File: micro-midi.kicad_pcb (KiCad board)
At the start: 2 copper layers, 36 x 39 mm, 14 parts, among them J1 AudioJack3, J2 Conn_01x04_Male, J3 AudioJack3, U1 74HC04, U2 6N137

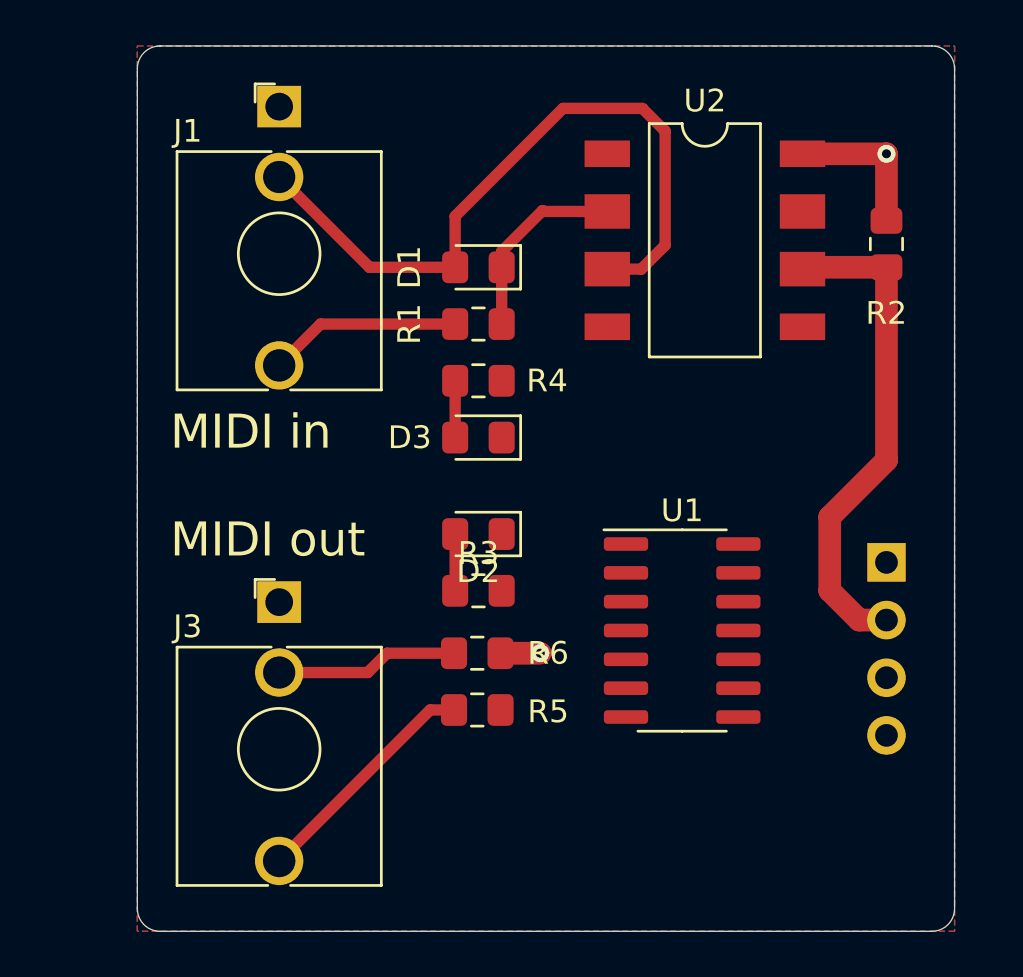
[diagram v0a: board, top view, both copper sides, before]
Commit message: finish pcb routing, clean up component numbers silkscreen
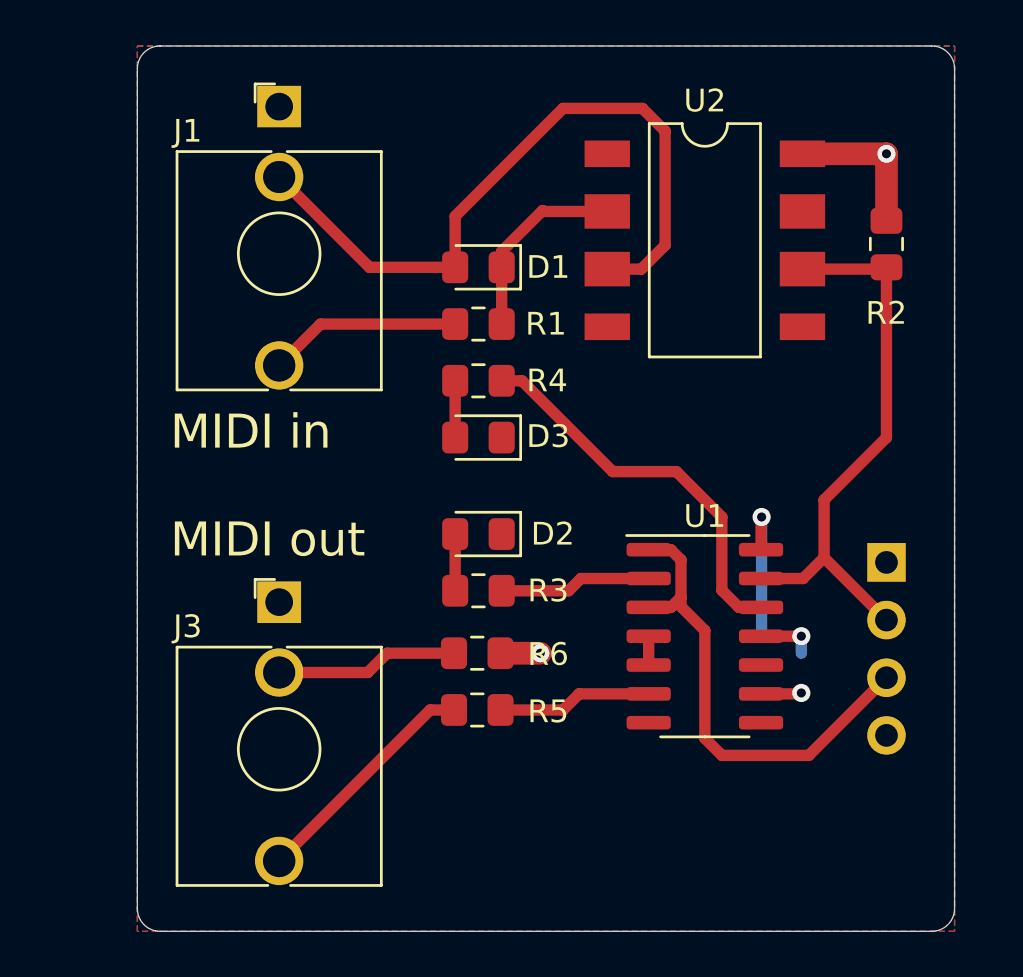
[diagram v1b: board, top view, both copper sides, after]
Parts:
- moved U1 1.03 mm to (98.0, 66.0)
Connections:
- U1 pad 12: (no net) -> Net-(R4-Pad2)
- U1 pad 13: +5V -> Net-(J2-Pad2)
- U1 pad 3: Net-(U1-Pad3) -> Net-(J2-Pad3)
- U1 pad 4: Net-(R5-Pad2) -> Net-(U1-Pad4)
- U1 pad 5: Net-(J2-Pad3) -> Net-(U1-Pad4)
- U1 pad 6: Net-(U1-Pad3) -> Net-(R5-Pad2)
- U1 pad 8: Net-(R4-Pad2) -> (no net)
- U1 pad 9: Net-(J2-Pad2) -> +5V
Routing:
- net Net-(J2-Pad3): track 0.00 -> 21.2 mm
- net Net-(R4-Pad2): track 0.00 -> 17.5 mm
- net +5V: track 8.40 -> 19.4 mm, vias 2 -> 5
- net Net-(R5-Pad2): track 0.00 -> 6.82 mm
- net Net-(R3-Pad2): track 0.00 -> 6.70 mm
- net Net-(J2-Pad2): track 22.0 -> 24.7 mm
- net Net-(U1-Pad4): track 0.00 -> 1.27 mm

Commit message: more compact component placement
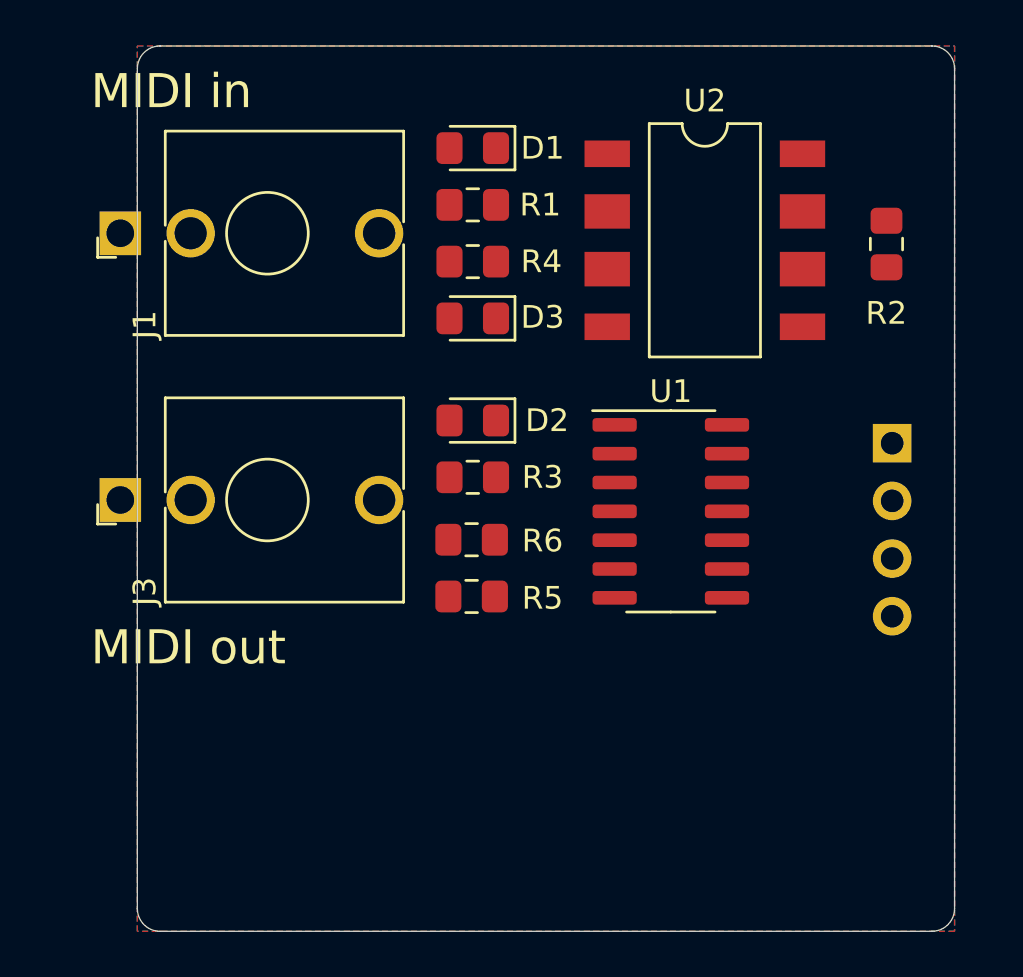
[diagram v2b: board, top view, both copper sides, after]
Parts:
- moved J1 8.95 mm to (72.2, 48.2), turned to 90 degrees
- moved J3 8.32 mm to (72.2, 60.0), turned to 90 degrees
- moved U1 5.70 mm to (96.5, 60.5)
- moved D1 5.26 mm to (87.8, 44.5)
- moved D3 5.26 mm to (87.8, 52.0)
- moved J2 5.26 mm to (106.2, 57.5)
- moved R1 5.26 mm to (87.8, 47.0)
- moved R4 5.26 mm to (87.8, 49.5)
- moved D2 5.01 mm to (87.8, 56.5)
- moved R3 5.01 mm to (87.8, 59.0)
- moved R5 5.01 mm to (87.7, 64.2)
- moved R6 5.01 mm to (87.7, 61.8)
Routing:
- net Net-(D1-Pad2): track 31.3 -> 0.00 mm
- net Net-(J2-Pad2): track 24.7 -> 0.00 mm
- net Net-(J2-Pad3): track 21.2 -> 0.00 mm
- net +5V: track 19.4 -> 0.00 mm, vias 5 -> 0
- net Net-(R4-Pad2): track 17.5 -> 0.00 mm
- net Net-(J3-PadT): track 10.5 -> 0.00 mm
- net Net-(D1-Pad1): track 8.61 -> 0.00 mm
- net Net-(J1-PadT): track 8.51 -> 0.00 mm
- net Net-(J3-PadR): track 8.05 -> 0.00 mm
- net Net-(R5-Pad2): track 6.82 -> 0.00 mm
- net Net-(R3-Pad2): track 6.70 -> 0.00 mm
- net Net-(D3-Pad2): track 2.50 -> 0.00 mm
- net Net-(D2-Pad2): track 2.50 -> 0.00 mm
- net Net-(U1-Pad4): track 1.27 -> 0.00 mm

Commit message: redo layout for smaller board
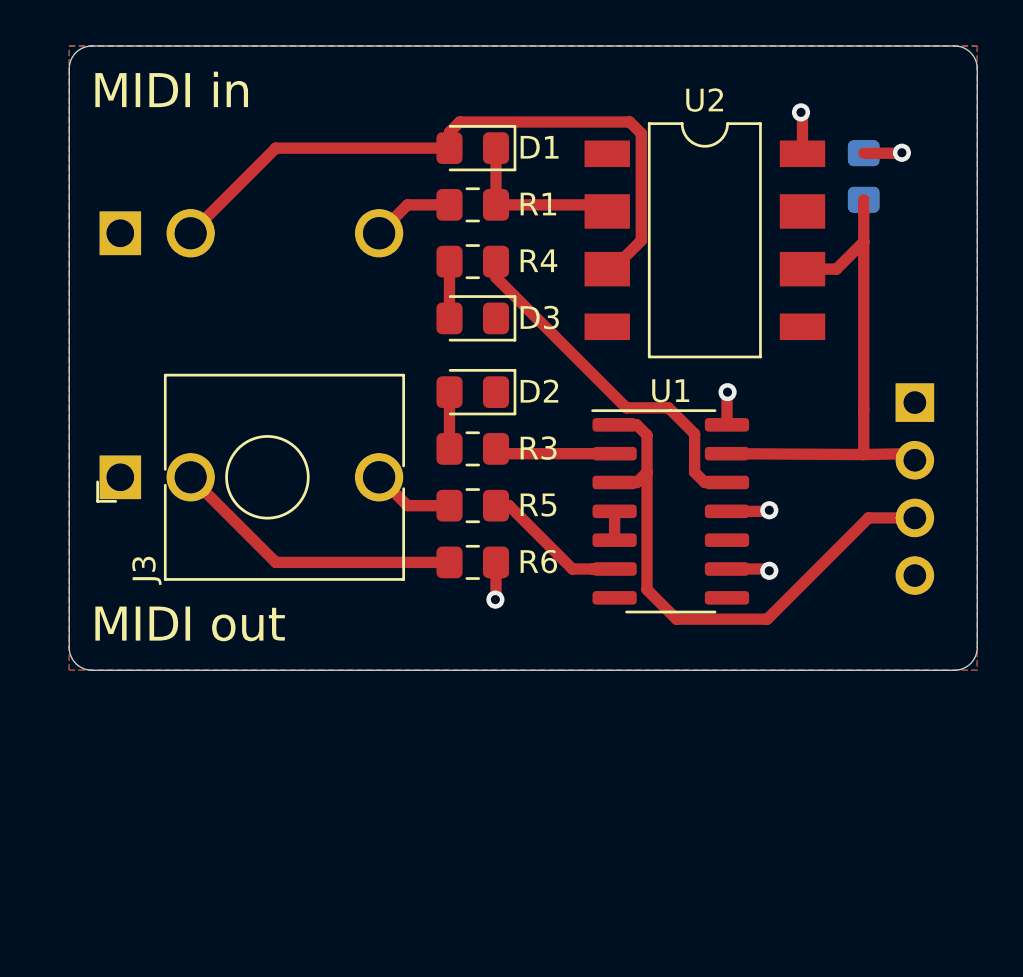
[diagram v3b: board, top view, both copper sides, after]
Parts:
- J1, R2: moved to B.Cu
- moved R5 4.00 mm to (87.8, 60.2)
- moved R2 3.14 mm to (105.0, 45.8), turned to 270 degrees
- moved J2 2.05 mm to (107.2, 55.7)
- moved D2 1.25 mm to (87.8, 55.2)
- moved R3 1.25 mm to (87.8, 57.8)
- moved R6 1.00 mm to (87.8, 62.8)
- moved J3 1.00 mm to (72.2, 59.0)
- turned J1 to 270 degrees
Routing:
- net Net-(D1-Pad2): track 0.00 -> 29.2 mm
- net Net-(J2-Pad3): track 0.00 -> 24.2 mm
- net Net-(J2-Pad2): track 0.00 -> 22.8 mm
- net Net-(R4-Pad2): track 0.00 -> 15.6 mm
- net Net-(J3-PadR): track 0.00 -> 13.0 mm
- net +5V: track 0.00 -> 10.4 mm, vias 0 -> 6
- net Net-(D1-Pad1): track 0.00 -> 7.52 mm
- net Net-(R5-Pad2): track 0.00 -> 6.38 mm
- net Net-(R3-Pad2): track 0.00 -> 5.31 mm
- net Net-(J3-PadT): track 0.00 -> 3.62 mm
- net Net-(J1-PadT): track 0.00 -> 3.62 mm
- net Net-(D3-Pad2): track 0.00 -> 2.50 mm
- net Net-(D2-Pad2): track 0.00 -> 2.50 mm
- net Net-(U1-Pad4): track 0.00 -> 1.27 mm
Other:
- board size 36 x 39 mm -> 40 x 27.5 mm
